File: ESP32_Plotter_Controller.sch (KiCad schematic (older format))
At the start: 43 parts, among them J1 ARM JTAG 10pin, J10 Pen Lift, J11 Vselect, J12 X Motor, J13 Y Motor, J14 Neo Pixel LEDs, J15 Pen Direction, J16 Aux Port (I2C), J17 USB_B_Micro, J18 E-Stop, J2 Power, J3 5V Aux, J4 Vin Aux, J5 Limit Switches, J6 Aux Port (SPI), J7 X Limit, J8 Micro_SD_Card_TF-01A, J9 Y Limit, SW1 RESET, SW2 BOOT, U1 ESP32-WROOM-32D, U2 TMC2130, U3 TMC2130, U4 XL1509, U5 CH340C, U6 AMS1117-3.3

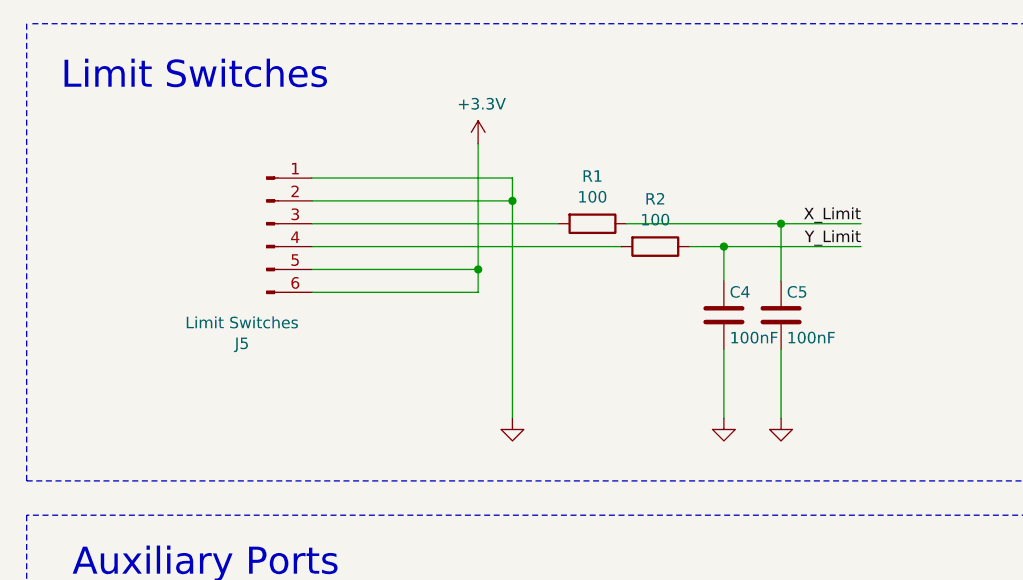
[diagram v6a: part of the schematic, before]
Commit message: Replace connectors with JST PH
Replace footprint associations with JST PH through hole right angle connectors and add associated LCSC part no (optimized for price and availability).
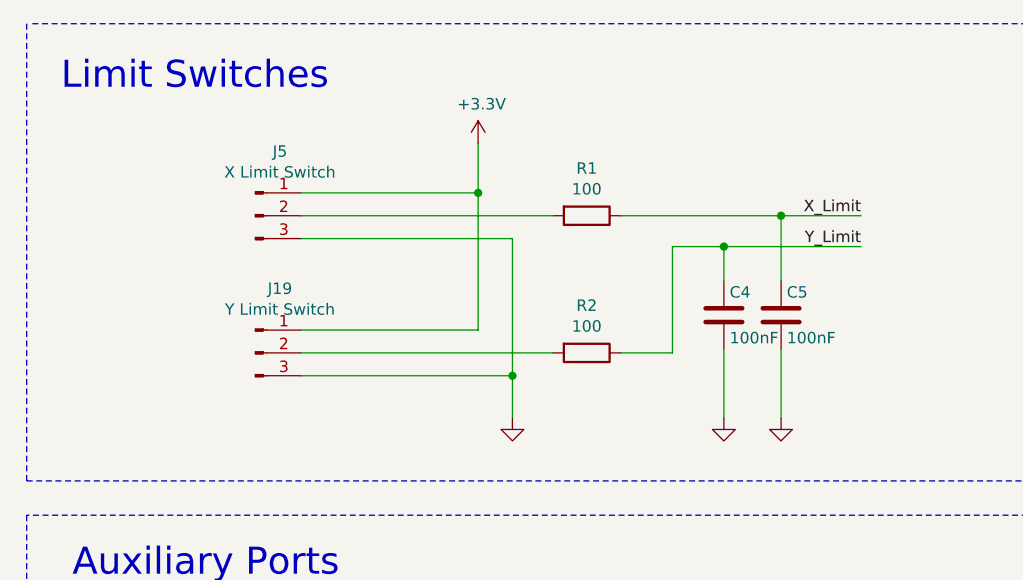
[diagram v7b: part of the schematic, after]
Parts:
- removed J5: Limit Switches, Connector_PinHeader_2.54mm:PinHeader_2x03_P2.54mm_Horizontal, symbol Connector:Conn_01x06_Male
- added J19: Y Limit Switch, Connector_JST:JST_PH_S3B-PH-K_1x03_P2.00mm_Horizontal, symbol Connector:Conn_01x03_Male
- added J5: X Limit Switch, Connector_JST:JST_PH_S3B-PH-K_1x03_P2.00mm_Horizontal, symbol Connector:Conn_01x03_Male
- J10, J14: footprint Connector_PinHeader_2.54mm:PinHeader_1x03_P2.54mm_Horizontal -> Connector_JST:JST_PH_S3B-PH-K_1x03_P2.00mm_Horizontal; LCSC (none) -> C10400 (JST PH TH RA)
- J12, J13: footprint Connector_PinHeader_2.54mm:PinHeader_1x04_P2.54mm_Horizontal -> Connector_JST:JST_PH_S4B-PH-K_1x04_P2.00mm_Horizontal; LCSC (none) -> C10401 JST PH TH RA
- J15, J18, J3, J4: footprint Connector_PinHeader_2.54mm:PinHeader_1x02_P2.54mm_Horizontal -> Connector_JST:JST_PH_S2B-PH-K_1x02_P2.00mm_Horizontal; LCSC (none) -> C16965 (JST PH TH RA)
- J16: footprint Connector_PinHeader_2.54mm:PinHeader_1x06_P2.54mm_Horizontal -> Connector_JST:JST_PH_S6B-PH-K_1x06_P2.00mm_Horizontal; LCSC (none) -> C5662 (JST PH TH RA)
- J6: footprint Connector_PinHeader_2.54mm:PinHeader_1x08_P2.54mm_Horizontal -> Connector_JST:JST_PH_S8B-PH-K_1x08_P2.00mm_Horizontal; LCSC (none) -> C14531 JST PH TH RA
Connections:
- net +3V3: now also J19.1 (Pin_1), J5.1 (Pin_1)
- net GND: now also J19.3 (Pin_3), J5.3 (Pin_3)
- net at R1.2: now also J5.2 (Pin_2)
- net at R2.2: now also J19.2 (Pin_2)
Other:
- moved on the sheet: R1, R2
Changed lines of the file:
@@
 	1800 6685 1800 6410
-$Comp
-L Connector:Conn_01x06_Male J5
-U 1 1 607F3660
-P 9700 1635
-F 0 "J5" H 9592 1110 50  0000 C CNN
-F 1 "Limit Switches" H 9592 1201 50  0000 C CNN
-F 2 "Connector_PinHeader_2.54mm:PinHeader_2x03_P2.54mm_Horizontal" H 9700 1635 50  0001 C CNN
-F 3 "~" H 9700 1635 50  0001 C CNN
-	1    9700 1635
-	1    0    0    -1
-$EndComp
-Wire Wire Line
-	9900 1435 10775 1435
-Wire Wire Line
-	10775 1435 10775 1535
-Wire Wire Line
-	9900 1935 10625 1935
-Wire Wire Line
-	9900 1835 10625 1835
-Wire Wire Line
-	10625 1835 10625 1935
-Wire Wire Line
-	9900 1635 10975 1635
-Wire Wire Line
-	9900 1735 11250 1735
 $Comp
 L Device:R R2
 U 1 1 6083E053
-P 11400 1735
-F 0 "R2" V 11193 1735 50  0000 C CNN
-F 1 "100" V 11284 1735 50  0000 C CNN
-F 2 "Resistor_SMD:R_0603_1608Metric" V 11330 1735 50  0001 C CNN
-F 3 "~" H 11400 1735 50  0001 C CNN
-	1    11400 1735
+P 11100 2200
+F 0 "R2" V 10893 2200 50  0000 C CNN
+F 1 "100" V 10984 2200 50  0000 C CNN
+F 2 "Resistor_SMD:R_0603_1608Metric" V 11030 2200 50  0001 C CNN
+F 3 "~" H 11100 2200 50  0001 C CNN
+	1    11100 2200
 	0    1    1    0
 $EndComp
@@
 L Device:R R1
 U 1 1 6083EB0D
-P 11125 1635
-F 0 "R1" V 10918 1635 50  0000 C CNN
-F 1 "100" V 11009 1635 50  0000 C CNN
-F 2 "Resistor_SMD:R_0603_1608Metric" V 11055 1635 50  0001 C CNN
-F 3 "~" H 11125 1635 50  0001 C CNN
-	1    11125 1635
+P 11100 1600
+F 0 "R1" V 10893 1600 50  0000 C CNN
+F 1 "100" V 10984 1600 50  0000 C CNN
+F 2 "Resistor_SMD:R_0603_1608Metric" V 11030 1600 50  0001 C CNN
+F 3 "~" H 11100 1600 50  0001 C CNN
+	1    11100 1600
 	0    1    1    0
 $EndComp
-Wire Wire Line
-	11550 1735 11700 1735
-Wire Wire Line
-	11275 1635 11950 1635
-Wire Wire Line
-	10775 1535 10775 2485
-Connection ~ 10775 1535
 Wire Wire Line
 	11950 2185 11950 2485
@@
 	11700 1885 11700 1735
 Connection ~ 11700 1735
-Wire Wire Line
-	11950 1885 11950 1635
-Connection ~ 11950 1635
-Text Label 12300 1635 2    50   ~ 0
-X_Limit
-Wire Wire Line
-	11950 1635 12300 1635
 Wire Wire Line
 	11700 1735 12300 1735
@@
 F 0 "J10" H 16233 7216 50  0000 C CNN
 F 1 "Pen Lift" H 16233 7125 50  0000 C CNN
-F 2 "Connector_PinHeader_2.54mm:PinHeader_1x03_P2.54mm_Horizontal" H 16125 6935 50  0001 C CNN
+F 2 "Connector_JST:JST_PH_S3B-PH-K_1x03_P2.00mm_Horizontal" H 16125 6935 50  0001 C CNN
 F 3 "~" H 16125 6935 50  0001 C CNN
+F 4 "C10400 (JST PH TH RA)" H 16125 6935 50  0001 C CNN "LCSC"
 	1    16125 6935
 	1    0    0    -1
@@
 F 0 "J12" H 18020 2430 50  0000 R CNN
 F 1 "X Motor" H 18140 2585 50  0000 R CNN
-F 2 "Connector_PinHeader_2.54mm:PinHeader_1x04_P2.54mm_Horizontal" H 17600 2535 50  0001 C CNN
+F 2 "Connector_JST:JST_PH_S4B-PH-K_1x04_P2.00mm_Horizontal" H 17600 2535 50  0001 C CNN
 F 3 "~" H 17600 2535 50  0001 C CNN
+F 4 "C10401 JST PH TH RA" H 17600 2535 50  0001 C CNN "LCSC"
 	1    17600 2535
 	1    0    0    -1
@@
 F 0 "J13" H 17975 4795 50  0000 R CNN
 F 1 "Y Motor" H 18155 4980 50  0000 R CNN
-F 2 "Connector_PinHeader_2.54mm:PinHeader_1x04_P2.54mm_Horizontal" H 17600 4935 50  0001 C CNN
+F 2 "Connector_JST:JST_PH_S4B-PH-K_1x04_P2.00mm_Horizontal" H 17600 4935 50  0001 C CNN
 F 3 "~" H 17600 4935 50  0001 C CNN
+F 4 "C10401 JST PH TH RA" H 17600 4935 50  0001 C CNN "LCSC"
 	1    17600 4935
 	1    0    0    -1
@@
 Text Notes 15000 12575 0    79   ~ 0
 ESP32 Plotter Controller\nDesign by Mark Benson github.com/markjb/ESP32_Plotter_Controller\nBased on Bart Drings ESP32 Pen Plotter Controller\nhttps://github.com/bdring/Grbl_ESP32_TMC2130_Plotter_Controller
-Wire Wire Line
-	10625 1835 10625 1285
-Connection ~ 10625 1835
 Wire Notes Line
 	8675 760  13575 760
@@
 F 0 "J6" H 9158 4766 50  0000 C CNN
 F 1 "Aux Port (SPI)" H 9158 4675 50  0000 C CNN
-F 2 "Connector_PinHeader_2.54mm:PinHeader_1x08_P2.54mm_Horizontal" H 9050 4285 50  0001 C CNN
+F 2 "Connector_JST:JST_PH_S8B-PH-K_1x08_P2.00mm_Horizontal" H 9050 4285 50  0001 C CNN
 F 3 "~" H 9050 4285 50  0001 C CNN
+F 4 "C14531 JST PH TH RA" H 9050 4285 50  0001 C CNN "LCSC"
 	1    9050 4285
 	1    0    0    -1
@@
 F 0 "J14" H 11678 4186 50  0000 C CNN
 F 1 "Neo Pixel LEDs" H 11678 4095 50  0000 C CNN
-F 2 "Connector_PinHeader_2.54mm:PinHeader_1x03_P2.54mm_Horizontal" H 11570 3905 50  0001 C CNN
+F 2 "Connector_JST:JST_PH_S3B-PH-K_1x03_P2.00mm_Horizontal" H 11570 3905 50  0001 C CNN
 F 3 "~" H 11570 3905 50  0001 C CNN
+F 4 "C10400 (JST PH TH RA)" H 11570 3905 50  0001 C CNN "LCSC"
 	1    11570 3905
 	1    0    0    -1
@@
 F 0 "J15" H 11678 4541 50  0000 C CNN
 F 1 "Pen Direction" H 11678 4450 50  0000 C CNN
-F 2 "Connector_PinHeader_2.54mm:PinHeader_1x02_P2.54mm_Horizontal" H 11570 4360 50  0001 C CNN
+F 2 "Connector_JST:JST_PH_S2B-PH-K_1x02_P2.00mm_Horizontal" H 11570 4360 50  0001 C CNN
 F 3 "~" H 11570 4360 50  0001 C CNN
+F 4 "C16965 (JST PH TH RA)" H 11570 4360 50  0001 C CNN "LCSC"
 	1    11570 4360
 	1    0    0    -1
@@
 F 0 "J16" H 9208 6141 50  0000 C CNN
 F 1 "Aux Port (I2C)" H 9208 6050 50  0000 C CNN
-F 2 "Connector_PinHeader_2.54mm:PinHeader_1x06_P2.54mm_Horizontal" H 9100 5760 50  0001 C CNN
+F 2 "Connector_JST:JST_PH_S6B-PH-K_1x06_P2.00mm_Horizontal" H 9100 5760 50  0001 C CNN
 F 3 "~" H 9100 5760 50  0001 C CNN
+F 4 "C5662 (JST PH TH RA)" H 9100 5760 50  0001 C CNN "LCSC"
 	1    9100 5760
 	1    0    0    -1
@@
 Wire Wire Line
 	11770 4005 12070 4005
-Wire Wire Line
-	9900 1535 10775 1535
 Wire Wire Line
 	10650 8510 9875 8510
@@
 F 0 "J4" H 2308 8266 50  0000 C CNN
 F 1 "Vin Aux" H 2308 8175 50  0000 C CNN
-F 2 "Connector_PinHeader_2.54mm:PinHeader_1x02_P2.54mm_Horizontal" H 2200 8085 50  0001 C CNN
+F 2 "Connector_JST:JST_PH_S2B-PH-K_1x02_P2.00mm_Horizontal" H 2200 8085 50  0001 C CNN
 F 3 "~" H 2200 8085 50  0001 C CNN
+F 4 "C16965 (JST PH TH RA)" H 2200 8085 50  0001 C CNN "LCSC"
 	1    2200 8085
 	1    0    0    -1
@@
 F 0 "J3" H 1558 8266 50  0000 C CNN
 F 1 "5V Aux" H 1425 8160 50  0000 C CNN
-F 2 "Connector_PinHeader_2.54mm:PinHeader_1x02_P2.54mm_Horizontal" H 1450 8085 50  0001 C CNN
+F 2 "Connector_JST:JST_PH_S2B-PH-K_1x02_P2.00mm_Horizontal" H 1450 8085 50  0001 C CNN
 F 3 "~" H 1450 8085 50  0001 C CNN
+F 4 "C16965 (JST PH TH RA)" H 1450 8085 50  0001 C CNN "LCSC"
 	1    1450 8085
 	1    0    0    -1
@@
 F 0 "J18" H 7128 3691 50  0000 C CNN
 F 1 "E-Stop" H 7128 3600 50  0000 C CNN
-F 2 "Connector_PinHeader_2.54mm:PinHeader_1x02_P2.54mm_Horizontal" H 7020 3510 50  0001 C CNN
+F 2 "Connector_JST:JST_PH_S2B-PH-K_1x02_P2.00mm_Horizontal" H 7020 3510 50  0001 C CNN
 F 3 "~" H 7020 3510 50  0001 C CNN
+F 4 "C16965 (JST PH TH RA)" H 7020 3510 50  0001 C CNN "LCSC"
 	1    7020 3510
 	1    0    0    -1
@@
 	1    0    0    -1
 $EndComp
+$Comp
+L Connector:Conn_01x03_Male J5
+U 1 1 6159A72B
+P 9650 1600
+F 0 "J5" H 9758 1881 50  0000 C CNN
+F 1 "X Limit Switch" H 9758 1790 50  0000 C CNN
+F 2 "Connector_JST:JST_PH_S3B-PH-K_1x03_P2.00mm_Horizontal" H 9650 1600 50  0001 C CNN
+F 3 "~" H 9650 1600 50  0001 C CNN
+F 4 "C10400 (JST PH TH RA)" H 9650 1600 50  0001 C CNN "LCSC"
+	1    9650 1600
+	1    0    0    -1
+$EndComp
+$Comp
+L Connector:Conn_01x03_Male J19
+U 1 1 6159BC1E
+P 9650 2200
+F 0 "J19" H 9758 2481 50  0000 C CNN
+F 1 "Y Limit Switch" H 9758 2390 50  0000 C CNN
+F 2 "Connector_JST:JST_PH_S3B-PH-K_1x03_P2.00mm_Horizontal" H 9650 2200 50  0001 C CNN
+F 3 "~" H 9650 2200 50  0001 C CNN
+F 4 "C10400 (JST PH TH RA)" H 9650 2200 50  0001 C CNN "LCSC"
+	1    9650 2200
+	1    0    0    -1
+$EndComp
+Wire Wire Line
+	10625 1285 10625 1500
+Wire Wire Line
+	9850 1500 10625 1500
+Connection ~ 10625 1500
+Wire Wire Line
+	9850 2100 10625 2100
+Wire Wire Line
+	10625 1500 10625 2100
+Wire Wire Line
+	9850 2300 10775 2300
+Connection ~ 10775 2300
+Wire Wire Line
+	10775 2300 10775 2485
+Wire Wire Line
+	9850 1700 10775 1700
+Wire Wire Line
+	10775 1700 10775 2300
+Wire Wire Line
+	9850 1600 10950 1600
+Wire Wire Line
+	9850 2200 10950 2200
+Wire Wire Line
+	11250 1600 11950 1600
+Text Label 12300 1600 2    50   ~ 0
+X_Limit
+Wire Wire Line
+	11950 1885 11950 1600
+Connection ~ 11950 1600
+Wire Wire Line
+	11950 1600 12300 1600
+Wire Wire Line
+	11475 1735 11475 2200
+Wire Wire Line
+	11475 2200 11250 2200
+Wire Wire Line
+	11475 1735 11700 1735
 $EndSCHEMATC

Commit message: Updated components etc
Used smaller buttons. Added custom footprint.
JST PH 2.0 thru-hole right angle connectors.
Connected USB 5v via diode to 3v3 regulator.
Silkscreen updated.
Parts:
- added D1: B5819W, Diode_SMD:D_SOD-123, symbol Device:D_Schottky
- J10: LCSC C10400 (JST PH TH RA) -> C10400 (JST PH TH RA) C10400 (JST PH TH RA) C395359 (JST PH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
- J14, J19, J5: LCSC C10400 (JST PH TH RA) -> C10400 (JST PH TH RA) C395359 (JST PH SMT RA)
- J15, J18, J3, J4: LCSC C16965 (JST PH TH RA) -> C16965 (JST PH TH RA), C47647 (JST PH SMT RA)
- J16: LCSC C5662 (JST PH TH RA) -> C5662 (JST PH TH RA) C395362 (JST PH SMT RA)
- J6: LCSC C14531 JST PH TH RA -> C14531 (JST PH TH RA) C519174 (JST PH SMT RA)
- SW1: footprint Button_Switch_SMD:SW_SPST_B3S-1000 -> custom:K2-1107ST; LCSC C127509 -> C127509 C118141 (smaller SMT)
- SW2: footprint Button_Switch_SMD:SW_SPST_B3S-1000 -> custom:K2-1107ST; LCSC (none) -> C127509 C118141 (smaller SMT)
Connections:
- net +5V: now also D1.1 (K)
- net at U2.11 (1B): now also J12.1 (Pin_1); no longer J12.4 (Pin_4)
- net at U2.12 (1A): now also J12.2 (Pin_2); no longer J12.3 (Pin_3)
- net at U2.13 (2A): now also J12.3 (Pin_3); no longer J12.2 (Pin_2)
- net at U2.14 (2B): now also J12.4 (Pin_4); no longer J12.1 (Pin_1)
- net at J13.1 (Pin_1): now also U3.11 (1B); no longer U3.14 (2B)
- net at J13.2 (Pin_2): now also U3.12 (1A); no longer U3.13 (2A)
- net at J13.3 (Pin_3): now also U3.13 (2A); no longer U3.12 (1A)
- net at J13.4 (Pin_4): now also U3.14 (2B); no longer U3.11 (1B)
- net at J17.1 (VBUS): now also D1.2 (A)
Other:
- moved on the sheet: J12, J13
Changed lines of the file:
@@
 F 2 "Connector_JST:JST_PH_S3B-PH-K_1x03_P2.00mm_Horizontal" H 16125 6935 50  0001 C CNN
 F 3 "~" H 16125 6935 50  0001 C CNN
-F 4 "C10400 (JST PH TH RA)" H 16125 6935 50  0001 C CNN "LCSC"
+F 4 "C10400 (JST PH TH RA) C10400 (JST PH TH RA) C395359 (JST PH SMT RA)" H 16125 6935 50  0001 C CNN "LCSC"
 	1    16125 6935
 	1    0    0    -1
@@
 L Connector:Conn_01x04_Male J12
 U 1 1 609055FD
-P 17600 2535
-F 0 "J12" H 18020 2430 50  0000 R CNN
-F 1 "X Motor" H 18140 2585 50  0000 R CNN
-F 2 "Connector_JST:JST_PH_S4B-PH-K_1x04_P2.00mm_Horizontal" H 17600 2535 50  0001 C CNN
-F 3 "~" H 17600 2535 50  0001 C CNN
-F 4 "C10401 JST PH TH RA" H 17600 2535 50  0001 C CNN "LCSC"
-	1    17600 2535
-	1    0    0    -1
+P 18000 2635
+F 0 "J12" H 18420 2530 50  0000 R CNN
+F 1 "X Motor" H 18540 2685 50  0000 R CNN
+F 2 "Connector_JST:JST_PH_S4B-PH-K_1x04_P2.00mm_Horizontal" H 18000 2635 50  0001 C CNN
+F 3 "~" H 18000 2635 50  0001 C CNN
+F 4 "C10401 JST PH TH RA" H 18000 2635 50  0001 C CNN "LCSC"
+	1    18000 2635
+	-1   0    0    1
 $EndComp
 $Comp
 L Connector:Conn_01x04_Male J13
 U 1 1 609064BE
-P 17600 4935
-F 0 "J13" H 17975 4795 50  0000 R CNN
-F 1 "Y Motor" H 18155 4980 50  0000 R CNN
-F 2 "Connector_JST:JST_PH_S4B-PH-K_1x04_P2.00mm_Horizontal" H 17600 4935 50  0001 C CNN
-F 3 "~" H 17600 4935 50  0001 C CNN
-F 4 "C10401 JST PH TH RA" H 17600 4935 50  0001 C CNN "LCSC"
-	1    17600 4935
-	1    0    0    -1
+P 18000 5035
+F 0 "J13" H 18375 4895 50  0000 R CNN
+F 1 "Y Motor" H 18555 5080 50  0000 R CNN
+F 2 "Connector_JST:JST_PH_S4B-PH-K_1x04_P2.00mm_Horizontal" H 18000 5035 50  0001 C CNN
+F 3 "~" H 18000 5035 50  0001 C CNN
+F 4 "C10401 JST PH TH RA" H 18000 5035 50  0001 C CNN "LCSC"
+	1    18000 5035
+	-1   0    0    1
 $EndComp
 Text Notes 15000 12575 0    79   ~ 0
@@
 F 2 "Connector_JST:JST_PH_S8B-PH-K_1x08_P2.00mm_Horizontal" H 9050 4285 50  0001 C CNN
 F 3 "~" H 9050 4285 50  0001 C CNN
-F 4 "C14531 JST PH TH RA" H 9050 4285 50  0001 C CNN "LCSC"
+F 4 "C14531 (JST PH TH RA) C519174 (JST PH SMT RA)" H 9050 4285 50  0001 C CNN "LCSC"
 	1    9050 4285
 	1    0    0    -1
@@
 F 2 "Connector_JST:JST_PH_S3B-PH-K_1x03_P2.00mm_Horizontal" H 11570 3905 50  0001 C CNN
 F 3 "~" H 11570 3905 50  0001 C CNN
-F 4 "C10400 (JST PH TH RA)" H 11570 3905 50  0001 C CNN "LCSC"
+F 4 "C10400 (JST PH TH RA) C395359 (JST PH SMT RA)" H 11570 3905 50  0001 C CNN "LCSC"
 	1    11570 3905
 	1    0    0    -1
@@
 F 2 "Connector_JST:JST_PH_S2B-PH-K_1x02_P2.00mm_Horizontal" H 11570 4360 50  0001 C CNN
 F 3 "~" H 11570 4360 50  0001 C CNN
-F 4 "C16965 (JST PH TH RA)" H 11570 4360 50  0001 C CNN "LCSC"
+F 4 "C16965 (JST PH TH RA), C47647 (JST PH SMT RA)" H 11570 4360 50  0001 C CNN "LCSC"
 	1    11570 4360
 	1    0    0    -1
@@
 F 2 "Connector_JST:JST_PH_S6B-PH-K_1x06_P2.00mm_Horizontal" H 9100 5760 50  0001 C CNN
 F 3 "~" H 9100 5760 50  0001 C CNN
-F 4 "C5662 (JST PH TH RA)" H 9100 5760 50  0001 C CNN "LCSC"
+F 4 "C5662 (JST PH TH RA) C395362 (JST PH SMT RA)" H 9100 5760 50  0001 C CNN "LCSC"
 	1    9100 5760
 	1    0    0    -1
@@
 F 2 "Connector_JST:JST_PH_S2B-PH-K_1x02_P2.00mm_Horizontal" H 2200 8085 50  0001 C CNN
 F 3 "~" H 2200 8085 50  0001 C CNN
-F 4 "C16965 (JST PH TH RA)" H 2200 8085 50  0001 C CNN "LCSC"
+F 4 "C16965 (JST PH TH RA), C47647 (JST PH SMT RA)" H 2200 8085 50  0001 C CNN "LCSC"
 	1    2200 8085
 	1    0    0    -1
@@
 F 2 "Connector_JST:JST_PH_S2B-PH-K_1x02_P2.00mm_Horizontal" H 1450 8085 50  0001 C CNN
 F 3 "~" H 1450 8085 50  0001 C CNN
-F 4 "C16965 (JST PH TH RA)" H 1450 8085 50  0001 C CNN "LCSC"
+F 4 "C16965 (JST PH TH RA), C47647 (JST PH SMT RA)" H 1450 8085 50  0001 C CNN "LCSC"
 	1    1450 8085
 	1    0    0    -1
@@
 F 0 "SW1" H 2000 4535 50  0000 C CNN
 F 1 "RESET" H 2000 4444 50  0000 C CNN
-F 2 "Button_Switch_SMD:SW_SPST_B3S-1000" H 2000 4450 50  0001 C CNN
+F 2 "custom:K2-1107ST" H 2000 4450 50  0001 C CNN
 F 3 "https://datasheet.lcsc.com/lcsc/1811082113_Korean-Hroparts-Elec-K2-1102SP-C4SC-04_C127509.pdf" H 2000 4450 50  0001 C CNN
-F 4 "C127509" H 2000 4250 50  0001 C CNN "LCSC"
+F 4 "C127509 C118141 (smaller SMT)" H 2000 4250 50  0001 C CNN "LCSC"
 	1    2000 4250
 	1    0    0    -1
@@
 F 0 "SW2" H 7325 4535 50  0000 C CNN
 F 1 "BOOT" H 7325 4444 50  0000 C CNN
-F 2 "Button_Switch_SMD:SW_SPST_B3S-1000" H 7325 4450 50  0001 C CNN
+F 2 "custom:K2-1107ST" H 7325 4450 50  0001 C CNN
 F 3 "~" H 7325 4450 50  0001 C CNN
+F 4 "C127509 C118141 (smaller SMT)" H 7325 4250 50  0001 C CNN "LCSC"
 	1    7325 4250
 	1    0    0    -1
@@
 F 2 "Connector_JST:JST_PH_S2B-PH-K_1x02_P2.00mm_Horizontal" H 7020 3510 50  0001 C CNN
 F 3 "~" H 7020 3510 50  0001 C CNN
-F 4 "C16965 (JST PH TH RA)" H 7020 3510 50  0001 C CNN "LCSC"
+F 4 "C16965 (JST PH TH RA), C47647 (JST PH SMT RA)" H 7020 3510 50  0001 C CNN "LCSC"
 	1    7020 3510
 	1    0    0    -1
@@
 F 2 "Connector_JST:JST_PH_S3B-PH-K_1x03_P2.00mm_Horizontal" H 9650 1600 50  0001 C CNN
 F 3 "~" H 9650 1600 50  0001 C CNN
-F 4 "C10400 (JST PH TH RA)" H 9650 1600 50  0001 C CNN "LCSC"
+F 4 "C10400 (JST PH TH RA) C395359 (JST PH SMT RA)" H 9650 1600 50  0001 C CNN "LCSC"
 	1    9650 1600
 	1    0    0    -1
@@
 F 2 "Connector_JST:JST_PH_S3B-PH-K_1x03_P2.00mm_Horizontal" H 9650 2200 50  0001 C CNN
 F 3 "~" H 9650 2200 50  0001 C CNN
-F 4 "C10400 (JST PH TH RA)" H 9650 2200 50  0001 C CNN "LCSC"
+F 4 "C10400 (JST PH TH RA) C395359 (JST PH SMT RA)" H 9650 2200 50  0001 C CNN "LCSC"
 	1    9650 2200
 	1    0    0    -1
@@
 Wire Wire Line
 	11475 1735 11700 1735
+$Comp
+L Device:D_Schottky D1
+U 1 1 61647E81
+P 3375 11075
+F 0 "D1" V 3329 11155 50  0000 L CNN
+F 1 "B5819W" V 3420 11155 50  0000 L CNN
+F 2 "Diode_SMD:D_SOD-123" H 3375 11075 50  0001 C CNN
+F 3 "https://datasheet.lcsc.com/szlcsc/Changjiang-Electronics-Tech-CJ-B5819W_C8598.pdf" H 3375 11075 50  0001 C CNN
+	1    3375 11075
+	0    1    1    0
+$EndComp
+$Comp
+L power:+5V #PWR0105
+U 1 1 61649438
+P 3375 10825
+F 0 "#PWR0105" H 3375 10675 50  0001 C CNN
+F 1 "+5V" H 3390 10998 50  0000 C CNN
+F 2 "" H 3375 10825 50  0001 C CNN
+F 3 "" H 3375 10825 50  0001 C CNN
+	1    3375 10825
+	1    0    0    -1
+$EndComp
+Wire Wire Line
+	3150 11350 3375 11350
+Wire Wire Line
+	3375 11225 3375 11350
+Wire Wire Line
+	3375 10925 3375 10825
 $EndSCHEMATC
